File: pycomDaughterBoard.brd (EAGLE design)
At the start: 42.9 x 43.2 mm, 15 parts, among them J2 VCC

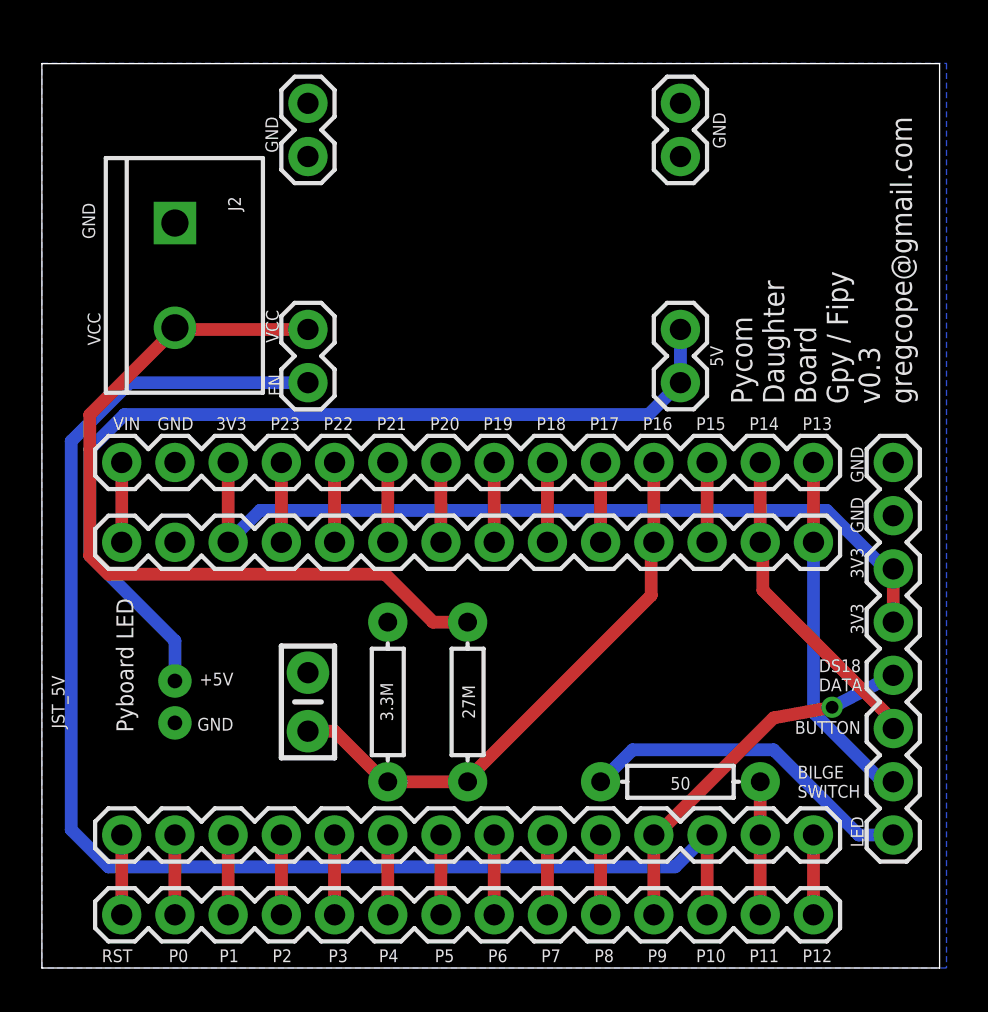
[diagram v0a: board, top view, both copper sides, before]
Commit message: v0.4 of board, with JSR headers
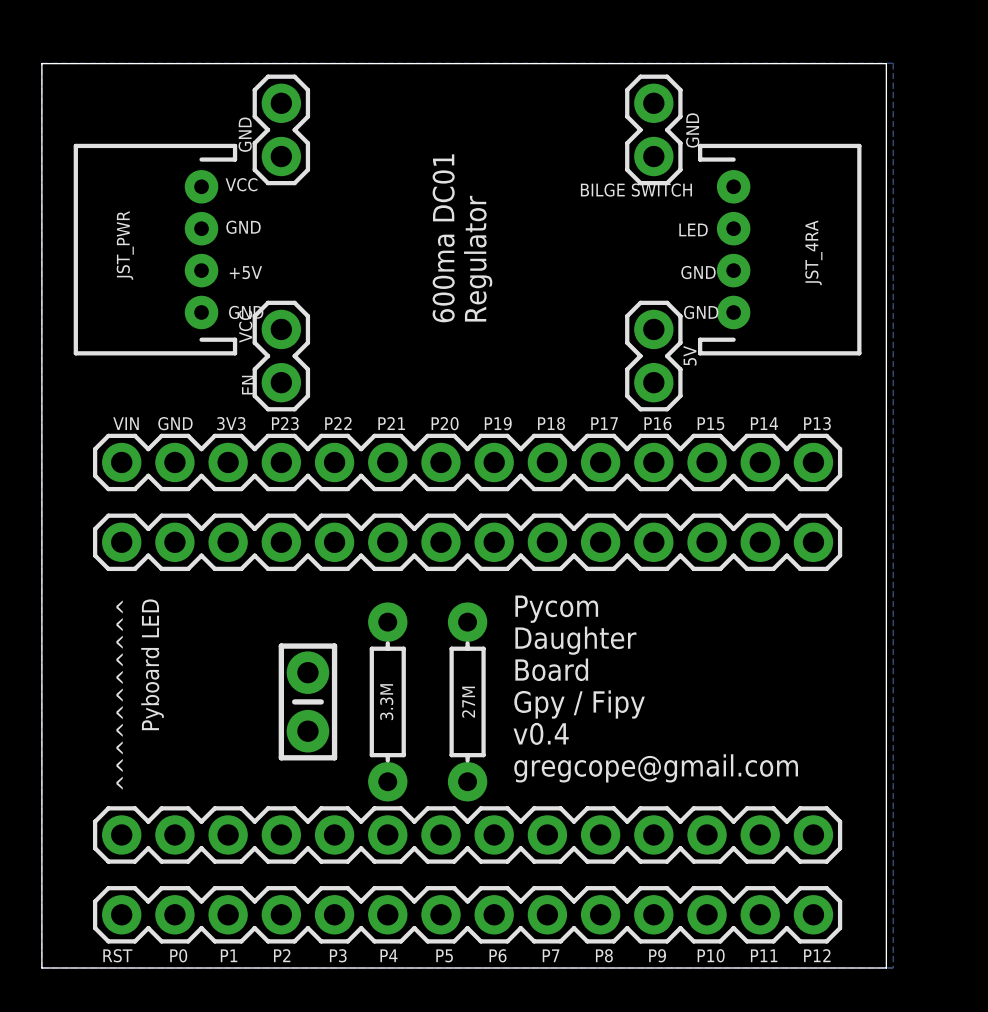
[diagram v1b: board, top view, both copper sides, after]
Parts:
- removed HEADER: J1, SparkFun-Connectors:1X08
- removed J2: VCC, SparkFun-Retired:SCREWTERMINAL-5MM-2
- removed JST_5V: 5v, SparkFun-Connectors:JST-2-PTH-NS
- removed R7: 50, SparkFun-Resistors:AXIAL-0.3
- added JST_4RA: PERPHS, SparkFun-Connectors:JST-4-PTH
- added JST_PWR: VVC_5V, SparkFun-Connectors:JST-4-PTH
- moved 5V 1.27 mm to (29.2, 27.9)
- moved GND 1.27 mm to (29.2, 38.7)
- moved GND_II 1.27 mm to (11.4, 41.3)
- moved VCC 1.27 mm to (11.4, 27.9)
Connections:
- removed net N$2: HEADER.1, R7.P$1
- net 3V3: no longer HEADER.5, HEADER.6
- net 5V: now also JST_PWR.2; no longer JST_5V.2
- net GND: now also JST_4RA.3, JST_4RA.4, JST_PWR.1, JST_PWR.3; no longer HEADER.7, HEADER.8, J2.1, JST_5V.1
- net P11: no longer R7.P$2
- net P13: now also JST_4RA.1; no longer HEADER.2
- net P14: now also JST_4RA.2; no longer HEADER.3
- net P9: no longer HEADER.4
- net VCC: now also JST_PWR.4; no longer J2.2
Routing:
- net P10: track 66.5 -> 0.00 mm
- net 5V: track 44.8 -> 0.00 mm
- net 3V3: track 39.9 -> 0.00 mm
- net VCC: track 38.3 -> 0.00 mm
- net P16: track 27.5 -> 0.00 mm
- net P9: track 18.0 -> 0.00 mm, vias 1 -> 0
- net P13: track 17.1 -> 0.00 mm
- net N$2: track 16.3 -> 0.00 mm
- net P14: track 15.3 -> 0.00 mm
- net P11: track 6.35 -> 0.00 mm
- net N$9: track 3.81 -> 0.00 mm
- net N$8: track 3.81 -> 0.00 mm
- net N$7: track 3.81 -> 0.00 mm
- net N$6: track 3.81 -> 0.00 mm
- net N$5: track 3.81 -> 0.00 mm
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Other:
- board size 42.9 x 43.2 mm -> 40.3 x 43.2 mm
- board text added: "600ma DC01 Regulator"
- board text added: "Pycom Daughter Board Gpy / Fipy v0.4 gregcope@gmail.com"
- board text added: "^^^^^^^^^^^ Pyboard LED"
- board text removed: "BUTTON"
- board text removed: "DS18 DATA"
- board text removed: "Pyboard LED"
- board text removed: "Pycom Daughter Board Gpy / Fipy v0.3 gregcope@gmail.com"

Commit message: Board v0.6 updates
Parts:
- removed R2: 27M, SparkFun-Resistors:AXIAL-0.3
- added R1: 27M, adafruit:0309/12
- moved C1 6.84 mm to (6.35, 15.2)
- moved R3 3.59 mm to (19.1, 15.2), turned to 0 degrees
- moved JST_4RA 1.27 mm to (31.8, 34.3)
- moved JST_PWR 1.27 mm to (8.89, 34.3)
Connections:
- net P16: now also R1.1; no longer R2.P$1
- net VCC: now also R1.2; no longer R2.P$2
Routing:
- net P10: track 0.00 -> 53.2 mm
- net VCC: track 0.00 -> 40.5 mm
- net P16: track 0.00 -> 32.6 mm
- net 5V: track 0.00 -> 24.0 mm
- net P13: track 0.00 -> 19.1 mm
- net P14: track 0.00 -> 16.1 mm
- net P9: track 0.00 -> 3.81 mm
- net P11: track 0.00 -> 3.81 mm
- net N$9: track 0.00 -> 3.81 mm
- net N$8: track 0.00 -> 3.81 mm
- net N$7: track 0.00 -> 3.81 mm
- net N$6: track 0.00 -> 3.81 mm
- net N$5: track 0.00 -> 3.81 mm
- net N$4: track 0.00 -> 3.81 mm
- net N$3: track 0.00 -> 3.81 mm
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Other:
- board text added: "Pycom Daughter Board Gpy / Fipy v0.6 gregcope@gmail.com"
- board text removed: "Pycom Daughter Board Gpy / Fipy v0.4 gregcope@gmail.com"
